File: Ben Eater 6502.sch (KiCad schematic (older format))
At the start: 24 parts, among them J1 PS/2 Keyboard, Q1 2N3906, SW1 Reset, SW2 NMI, U1 W65C02SxP, U2 4011, U3 28C256, U4 AS6C62256A, U5 W65C22SxP, U6 74HC74, U7 74HC595, U8 74HC595

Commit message: Stage 7
Add some missing pullup/pulldown resistors
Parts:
- added R9: 4K7, symbol Device:R
- R1, R4: value R -> 10K
- R2, R3, R5, R6: value R -> 4K7
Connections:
- net +5V: now also R9.1
- net SR_~OE~: now also R9.2
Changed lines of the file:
@@
 P 3700 1625
 F 0 "R1" H 3770 1671 50  0000 L CNN
-F 1 "R" H 3770 1580 50  0000 L CNN
+F 1 "10K" H 3770 1580 50  0000 L CNN
 F 2 "" V 3630 1625 50  0001 C CNN
 F 3 "~" H 3700 1625 50  0001 C CNN
@@
 P 3300 2425
 F 0 "R4" H 3370 2471 50  0000 L CNN
-F 1 "R" H 3370 2380 50  0000 L CNN
+F 1 "10K" H 3370 2380 50  0000 L CNN
 F 2 "" V 3230 2425 50  0001 C CNN
 F 3 "~" H 3300 2425 50  0001 C CNN
@@
 P 7600 4900
 F 0 "R3" V 7393 4900 50  0000 C CNN
-F 1 "R" V 7484 4900 50  0000 C CNN
+F 1 "4K7" V 7484 4900 50  0000 C CNN
 F 2 "" V 7530 4900 50  0001 C CNN
 F 3 "~" H 7600 4900 50  0001 C CNN
@@
 P 3100 3325
 F 0 "R2" V 2875 3275 50  0000 L CNN
-F 1 "R" V 2975 3300 50  0000 L CNN
+F 1 "4K7" V 2975 3250 50  0000 L CNN
 F 2 "" V 3030 3325 50  0001 C CNN
 F 3 "~" H 3100 3325 50  0001 C CNN
@@
 P 3100 3425
 F 0 "R6" V 2875 3375 50  0000 L CNN
-F 1 "R" V 2975 3400 50  0000 L CNN
+F 1 "4K7" V 2975 3350 50  0000 L CNN
 F 2 "" V 3030 3425 50  0001 C CNN
 F 3 "~" H 3100 3425 50  0001 C CNN
@@
 P 7975 4900
 F 0 "R5" V 7768 4900 50  0000 C CNN
-F 1 "R" V 7859 4900 50  0000 C CNN
+F 1 "4K7" V 7859 4900 50  0000 C CNN
 F 2 "" V 7905 4900 50  0001 C CNN
 F 3 "~" H 7975 4900 50  0001 C CNN
@@
 Wire Wire Line
 	4175 9400 4225 9400
+$Comp
+L Device:R R9
+U 1 1 61216BE2
+P 3000 8850
+F 0 "R9" V 2793 8850 50  0000 C CNN
+F 1 "4K7" V 2884 8850 50  0000 C CNN
+F 2 "" V 2930 8850 50  0001 C CNN
+F 3 "~" H 3000 8850 50  0001 C CNN
+	1    3000 8850
+	-1   0    0    1
+$EndComp
+Text GLabel 3075 9100 2    50   Input ~ 0
+H
+Wire Wire Line
+	3000 8700 3000 8600
+Connection ~ 3000 8600
+Wire Wire Line
+	3000 9000 3000 9100
+Wire Wire Line
+	3000 9100 3075 9100
 Wire Bus Line
 	9450 1150 9450 2825

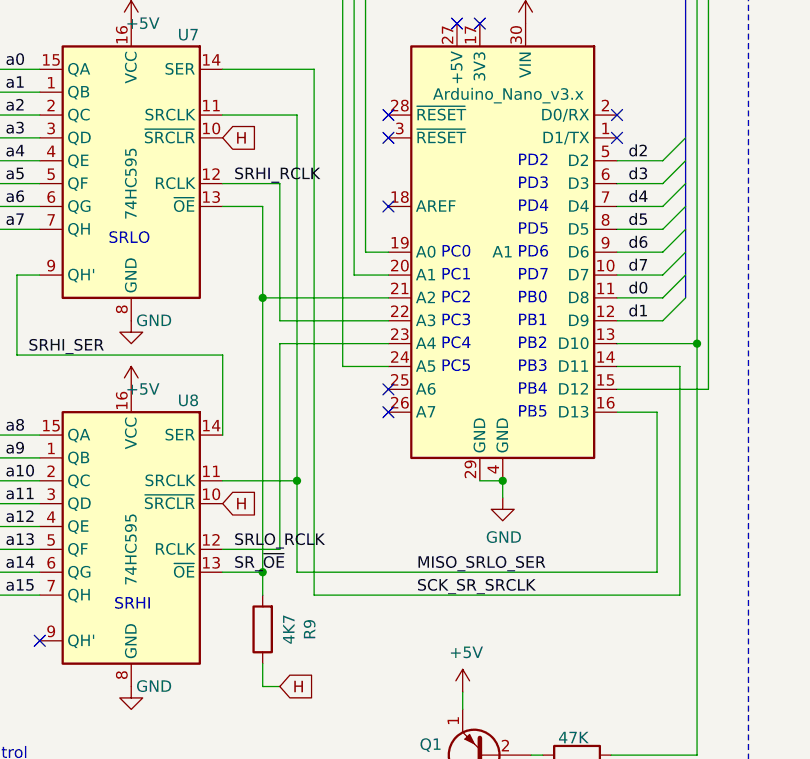
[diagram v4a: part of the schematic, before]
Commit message: Fix buggy net labels
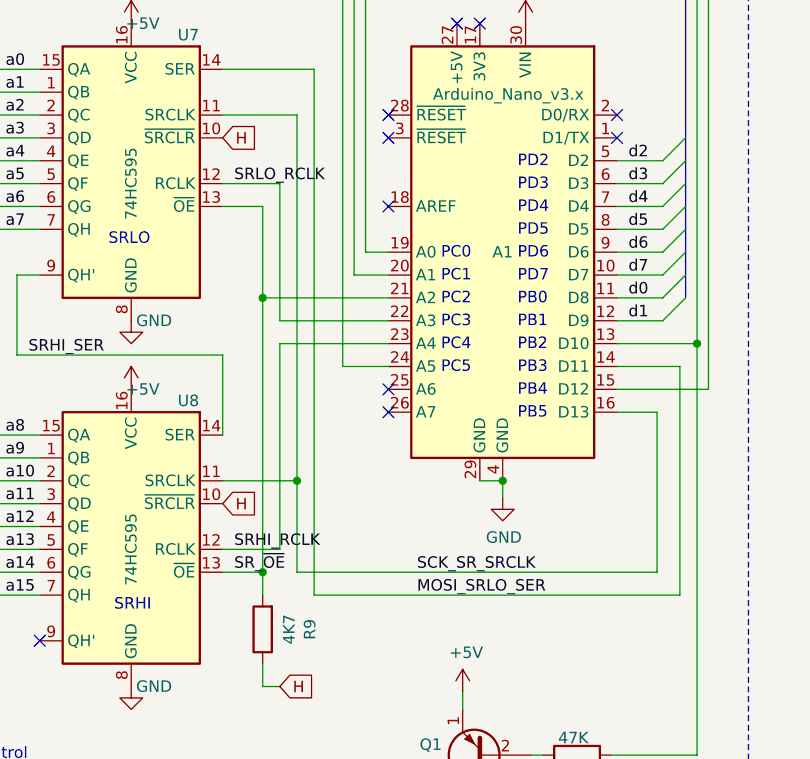
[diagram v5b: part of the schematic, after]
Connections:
- net MISO_SRLO_SER is gone; now on net SCK_SR_SRCLK: A1.16 (D13), U7.11 (SRCLK), U8.11 (SRCLK)
- net SCK_SR_SRCLK: no longer A1.14 (D11), U7.14 (SER)
- net SRHI_RCLK: now also A1.23 (A4), U8.12 (RCLK); no longer A1.22 (A3), U7.12 (RCLK)
- net SRLO_RCLK: now also A1.22 (A3), U7.12 (RCLK); no longer A1.23 (A4), U8.12 (RCLK)
- new net MOSI_SRLO_SER: A1.14 (D11), U7.14 (SER)
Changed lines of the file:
@@
 	4725 7900 4725 8600
 Connection ~ 5200 1150
+Text Label 3675 8700 0    50   ~ 0
+MOSI_SRLO_SER
 Text Label 3675 8600 0    50   ~ 0
-MISO_SRLO_SER
-Text Label 3675 8700 0    50   ~ 0
 SCK_SR_SRCLK
 Wire Wire Line
@@
 SRHI_SER
 Text Label 2875 6900 0    50   ~ 0
+SRLO_RCLK
+Text Label 2875 8500 0    50   ~ 0
 SRHI_RCLK
-Text Label 2875 8500 0    50   ~ 0
-SRLO_RCLK
 Text Label 2875 8600 0    50   ~ 0
 SR_~OE~

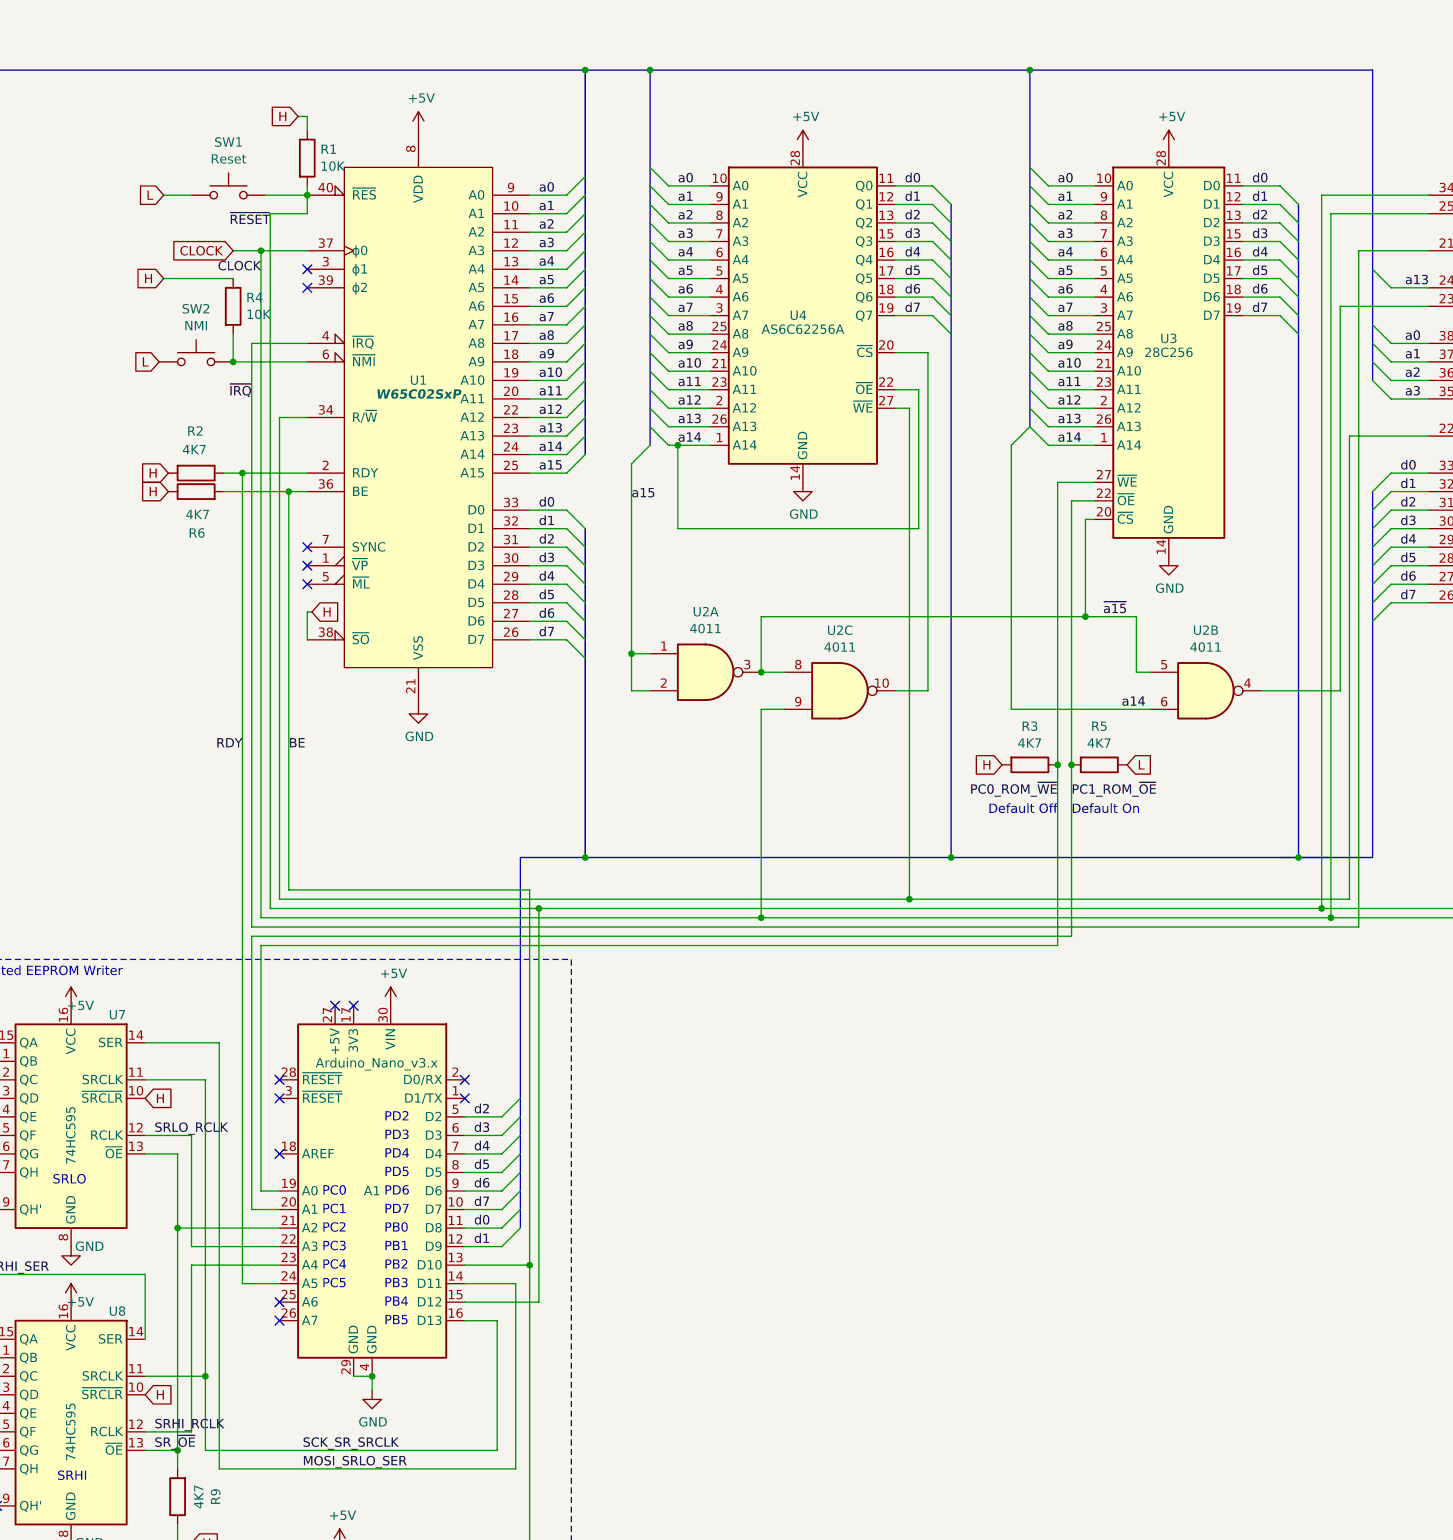
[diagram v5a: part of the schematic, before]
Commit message: Add reset circuit
From https://wilsonminesco.com/6502primer/RSTreqs.html

Old reset button and arduino reset lines updated accordingly
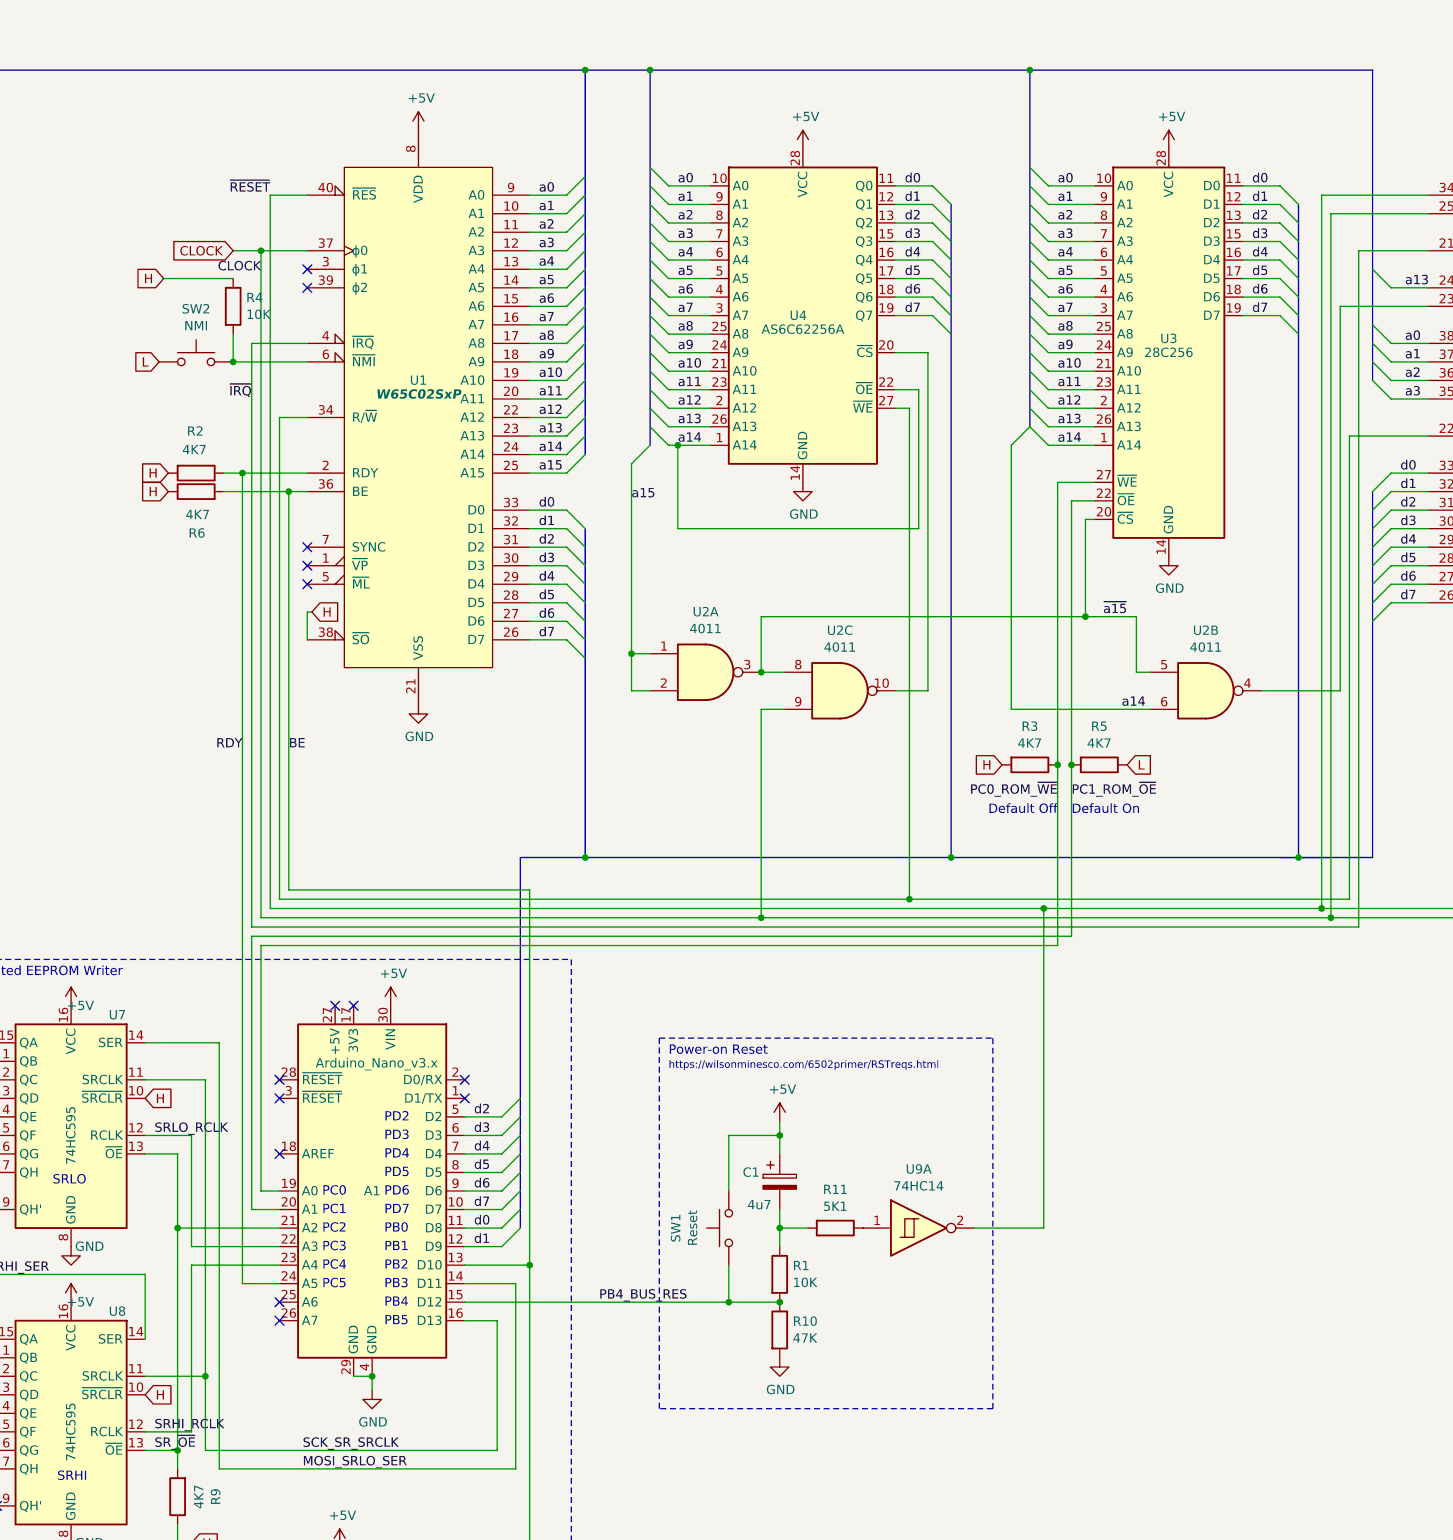
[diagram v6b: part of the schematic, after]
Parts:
- added C1: 4u7, symbol Device:CP
- added R10: 47K, symbol Device:R
- added R11: 5K1, symbol Device:R
- added U9: 74HC14, symbol 74xx:74HC14
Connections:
- net +5V: now also SW1.2, C1.1; no longer R1.1
- net GND: now also R10.2; no longer SW1.1
- net ~RESET~: now also U9.2; no longer A1.15 (D12), R1.2, SW1.2
- new net: C1.2, R1.1, R11.2
- new net: R11.1, U9.1
- new net PB4_BUS_RES: A1.15 (D12), R1.2, R10.1, SW1.1
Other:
- note added: "Power-on Reset"
- note added: "https://wilsonminesco.com/6502primer/RSTreqs.html"
- moved on the sheet: R1, SW1
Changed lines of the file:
@@
 encoding utf-8
 Sheet 1 1
-Title "Ben Eater 6502 - Stage 7"
+Title "Ben Eater 6502 - Stage 8"
 Date "2021-03-22"
 Rev ""
@@
 L Switch:SW_Push SW1
 U 1 1 6058FD77
-P 3275 1825
-F 0 "SW1" H 3275 2110 50  0000 C CNN
-F 1 "Reset" H 3275 2019 50  0000 C CNN
-F 2 "" H 3275 2025 50  0001 C CNN
-F 3 "~" H 3275 2025 50  0001 C CNN
-	1    3275 1825
-	1    0    0    -1
-$EndComp
-Text GLabel 2925 1825 0    50   Input ~ 0
-L
+P 5975 7400
+F 0 "SW1" H 5975 7685 50  0000 C CNN
+F 1 "Reset" H 5975 7594 50  0000 C CNN
+F 2 "" H 5975 7600 50  0001 C CNN
+F 3 "~" H 5975 7600 50  0001 C CNN
+	1    5975 7400
+	0    -1   -1   0
+$EndComp
 $Comp
 L Device:R R1
 U 1 1 605910CF
-P 3700 1625
-F 0 "R1" H 3770 1671 50  0000 L CNN
-F 1 "10K" H 3770 1580 50  0000 L CNN
-F 2 "" V 3630 1625 50  0001 C CNN
-F 3 "~" H 3700 1625 50  0001 C CNN
-	1    3700 1625
-	1    0    0    -1
-$EndComp
-Wire Wire Line
-	3700 1400 3700 1475
-Wire Wire Line
-	3700 1775 3700 1825
+P 6250 7650
+F 0 "R1" H 6320 7696 50  0000 L CNN
+F 1 "10K" H 6320 7605 50  0000 L CNN
+F 2 "" V 6180 7650 50  0001 C CNN
+F 3 "~" H 6250 7650 50  0001 C CNN
+	1    6250 7650
+	1    0    0    -1
+$EndComp
 Text GLabel 3300 2125 0    50   Input ~ 0
 CLOCK
@@
 	1    0    0    -1
 $EndComp
-Connection ~ 3700 1825
 $Comp
 L 4xxx:4011 U2
@@
 Wire Wire Line
 	3700 3025 3550 3025
-Wire Wire Line
-	3700 1825 3700 1925
-Wire Wire Line
-	3700 1925 3500 1925
-Wire Wire Line
-	3500 1925 3500 5675
 Wire Wire Line
 	3700 2125 3450 2125
@@
 Text GLabel 2950 3325 0    50   Input ~ 0
 H
-Text GLabel 3650 1400 0    50   Input ~ 0
-H
-Wire Wire Line
-	3700 1400 3650 1400
 $Comp
 L Display_Character:WC1602A DS1
@@
 Wire Wire Line
 	12000 5000 11475 5000
-Wire Wire Line
-	3500 5675 4950 5675
 Connection ~ 9175 5675
 Wire Wire Line
@@
 Default On\n
 Connection ~ 14100 8575
-Wire Wire Line
-	3700 1825 3475 1825
-Wire Wire Line
-	3075 1825 2925 1825
 $Comp
 L Device:R R2
@@
 $EndComp
 Wire Wire Line
-	4550 7800 4950 7800
-Wire Wire Line
-	4950 7800 4950 5675
-Wire Wire Line
 	3700 4225 3700 4075
 Wire Wire Line
@@
 Wire Wire Line
 	3600 5575 4900 5575
-Connection ~ 4950 5675
-Wire Wire Line
-	4950 5675 9175 5675
 Wire Bus Line
 	4850 5400 5200 5400
@@
 	3600 3425 3250 3425
 Connection ~ 3600 3425
-Text Label 3500 2000 2    50   ~ 0
+Text Label 3500 1825 2    50   ~ 0
 ~RESET~
 Text Label 3450 2250 2    50   ~ 0
@@
 Wire Wire Line
 	3000 9100 3075 9100
+$Comp
+L 74xx:74HC14 U9
+U 1 1 6124308A
+P 7000 7400
+F 0 "U9" H 7000 7717 50  0000 C CNN
+F 1 "74HC14" H 7000 7626 50  0000 C CNN
+F 2 "" H 7000 7400 50  0001 C CNN
+F 3 "http://www.ti.com/lit/gpn/sn74HC14" H 7000 7400 50  0001 C CNN
+	1    7000 7400
+	1    0    0    -1
+$EndComp
+Wire Wire Line
+	3500 1825 3700 1825
+Wire Wire Line
+	3500 1825 3500 5675
+$Comp
+L Device:R R11
+U 1 1 612925DE
+P 6550 7400
+F 0 "R11" V 6343 7400 50  0000 C CNN
+F 1 "5K1" V 6434 7400 50  0000 C CNN
+F 2 "" V 6480 7400 50  0001 C CNN
+F 3 "~" H 6550 7400 50  0001 C CNN
+	1    6550 7400
+	0    1    1    0
+$EndComp
+$Comp
+L Device:CP C1
+U 1 1 61293C4F
+P 6250 7150
+F 0 "C1" H 6050 7200 50  0000 L CNN
+F 1 "4u7" H 6075 7025 50  0000 L CNN
+F 2 "" H 6288 7000 50  0001 C CNN
+F 3 "~" H 6250 7150 50  0001 C CNN
+	1    6250 7150
+	1    0    0    -1
+$EndComp
+$Comp
+L power:+5V #PWR021
+U 1 1 61295BBF
+P 6250 6825
+F 0 "#PWR021" H 6250 6675 50  0001 C CNN
+F 1 "+5V" H 6265 6998 50  0000 C CNN
+F 2 "" H 6250 6825 50  0001 C CNN
+F 3 "" H 6250 6825 50  0001 C CNN
+	1    6250 6825
+	1    0    0    -1
+$EndComp
+$Comp
+L Device:R R10
+U 1 1 61298039
+P 6250 7950
+F 0 "R10" H 6320 7996 50  0000 L CNN
+F 1 "47K" H 6320 7905 50  0000 L CNN
+F 2 "" V 6180 7950 50  0001 C CNN
+F 3 "~" H 6250 7950 50  0001 C CNN
+	1    6250 7950
+	1    0    0    -1
+$EndComp
+Wire Wire Line
+	6250 6900 6250 6825
+Wire Wire Line
+	6250 7000 6250 6900
+Connection ~ 6250 6900
+Wire Wire Line
+	6250 7300 6250 7400
+Wire Wire Line
+	6250 7400 6400 7400
+Wire Wire Line
+	5975 7200 5975 6900
+Wire Wire Line
+	5975 6900 6250 6900
+Wire Wire Line
+	5975 7600 5975 7800
+Wire Wire Line
+	5975 7800 6250 7800
+Connection ~ 6250 7800
+$Comp
+L power:GND #PWR022
+U 1 1 613E0528
+P 6250 8100
+F 0 "#PWR022" H 6250 7850 50  0001 C CNN
+F 1 "GND" H 6255 7927 50  0000 C CNN
+F 2 "" H 6250 8100 50  0001 C CNN
+F 3 "" H 6250 8100 50  0001 C CNN
+	1    6250 8100
+	1    0    0    -1
+$EndComp
+Wire Wire Line
+	6250 7500 6250 7400
+Connection ~ 6250 7400
+Wire Wire Line
+	4550 7800 5975 7800
+Wire Wire Line
+	3500 5675 7675 5675
+Connection ~ 5975 7800
+Wire Wire Line
+	7675 7400 7675 5675
+Wire Wire Line
+	7300 7400 7675 7400
+Connection ~ 7675 5675
+Wire Wire Line
+	7675 5675 9175 5675
+Text Label 5275 7800 0    50   ~ 0
+PB4_BUS_RES
+Wire Notes Line
+	5600 6375 7400 6375
+Wire Notes Line
+	7400 6375 7400 8375
+Wire Notes Line
+	7400 8375 5600 8375
+Wire Notes Line
+	5600 8375 5600 6375
+Text Notes 5650 6475 0    50   ~ 0
+Power-on Reset
+Text Notes 5650 6550 0    40   ~ 0
+https://wilsonminesco.com/6502primer/RSTreqs.html
 Wire Bus Line
 	9450 1150 9450 2825
